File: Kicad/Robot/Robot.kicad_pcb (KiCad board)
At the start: 2 copper layers, 159 x 78.5 mm, 55 parts, among them J1 PositiveBus, J10 LORA, J11 RELAY HEADER, J12 X8R HEADER, J13 SENSOR 1, J14 SENSOR 2, J15 SENSOR 3, J16 SENSOR 4, J2 NegativeBus, J3 PIN HEADER DE0-NANO POWER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

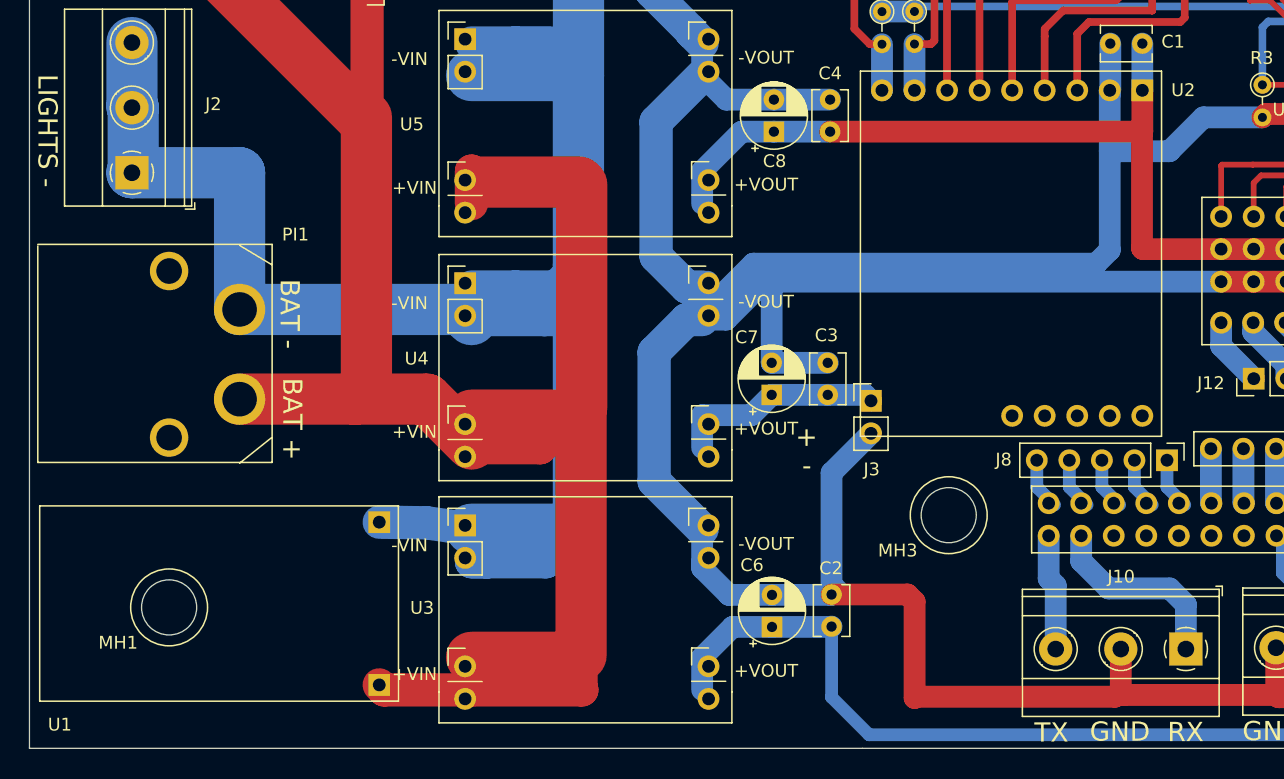
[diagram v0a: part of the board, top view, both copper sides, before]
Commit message: fixed usb polarity, added usb 3d model, edited usb footprin for flush mounting, updated pictures
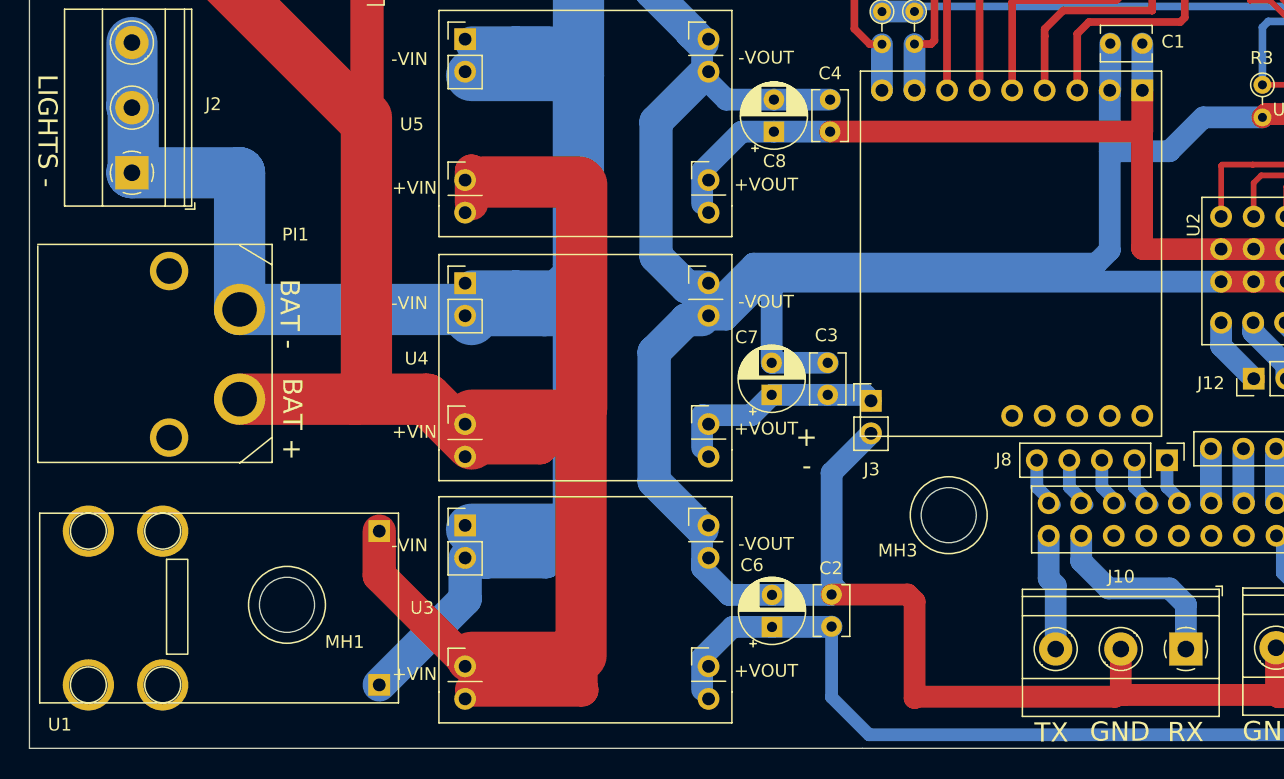
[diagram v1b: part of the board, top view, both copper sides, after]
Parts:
- moved MH1 9.20 mm to (-43.9, 52.8)
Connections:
- U1 pad 1: Net-(J1-Pad1) -> Net-(J2-Pad1)
- U1 pad 2: Net-(J2-Pad1) -> Net-(J1-Pad1)
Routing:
- net Net-(J1-Pad1): track 206.5 -> 212.5 mm
- net Net-(J2-Pad1): track 197.5 -> 202.9 mm
